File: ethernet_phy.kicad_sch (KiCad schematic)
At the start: 25 parts, among them J2 RJ45_Abracon_ARJP11A-MASA-B-A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, U1 RTL8201F

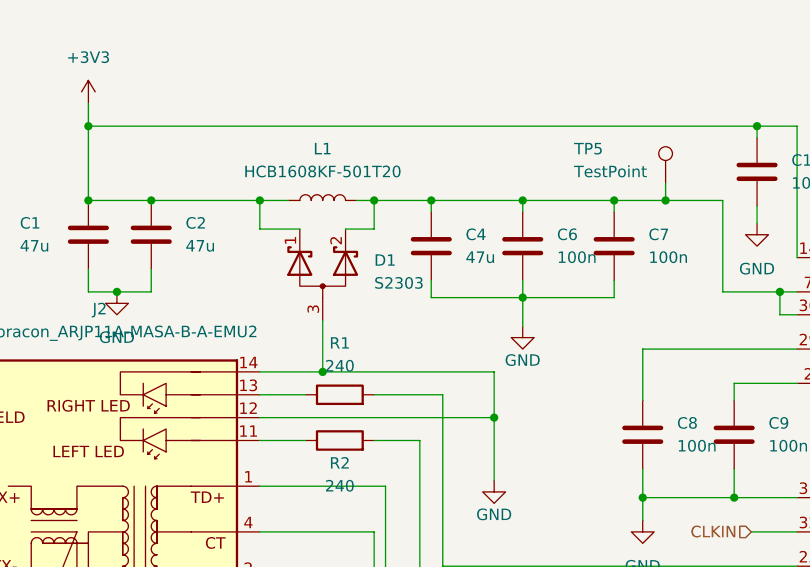
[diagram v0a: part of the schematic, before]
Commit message: Add more LCSC markings, change to electrolytic caps :
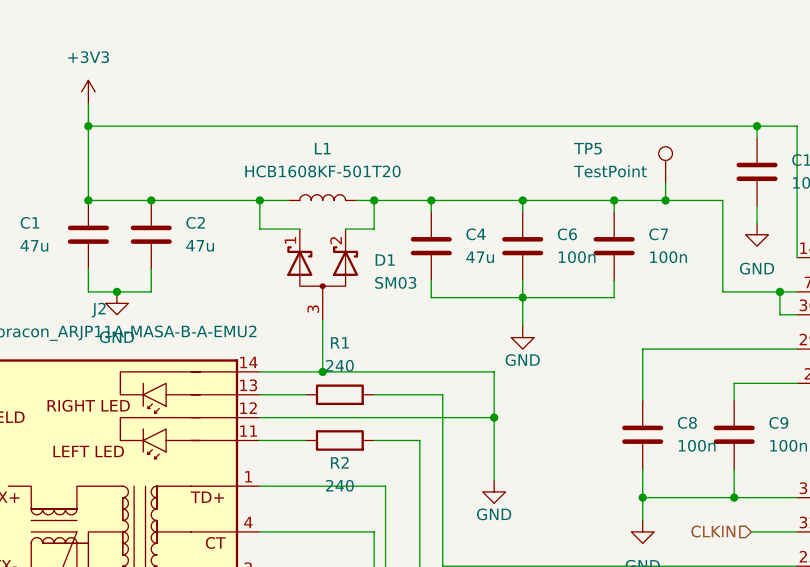
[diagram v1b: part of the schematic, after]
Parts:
- D1: value S2303 -> SM03; LCSC (none) -> C502558
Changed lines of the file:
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@@
       (effects (font (size 1.27 1.27)) (justify right))
     )
-    (property "Value" "S2303" (id 1) (at 92.075 57.4674 90)
+    (property "Value" "SM03" (id 1) (at 92.075 57.4674 90)
       (effects (font (size 1.27 1.27)) (justify right))
     )
@@
       (effects (font (size 1.27 1.27)) hide)
     )
-    (property "Datasheet" "https://www.smc-diodes.com/propdf/S2303%20THRU%20S2336%20N0291%20REV.B.pdf" (id 3) (at 86.36 57.785 0)
+    (property "Datasheet" "https://datasheet.lcsc.com/lcsc/2004071010_MDD-Microdiode-Electronics--SM03_C502558.pdf" (id 3) (at 86.36 57.785 0)
       (effects (font (size 1.27 1.27)) hide)
     )
+    (property "LCSC" "C502558" (id 4) (at 86.36 56.515 90)
+      (effects (font (size 1.27 1.27)) hide)
+    )
+    (property "Field5" "" (id 5) (at 86.36 56.515 90)
+      (effects (font (size 1.27 1.27)) hide)
+    )

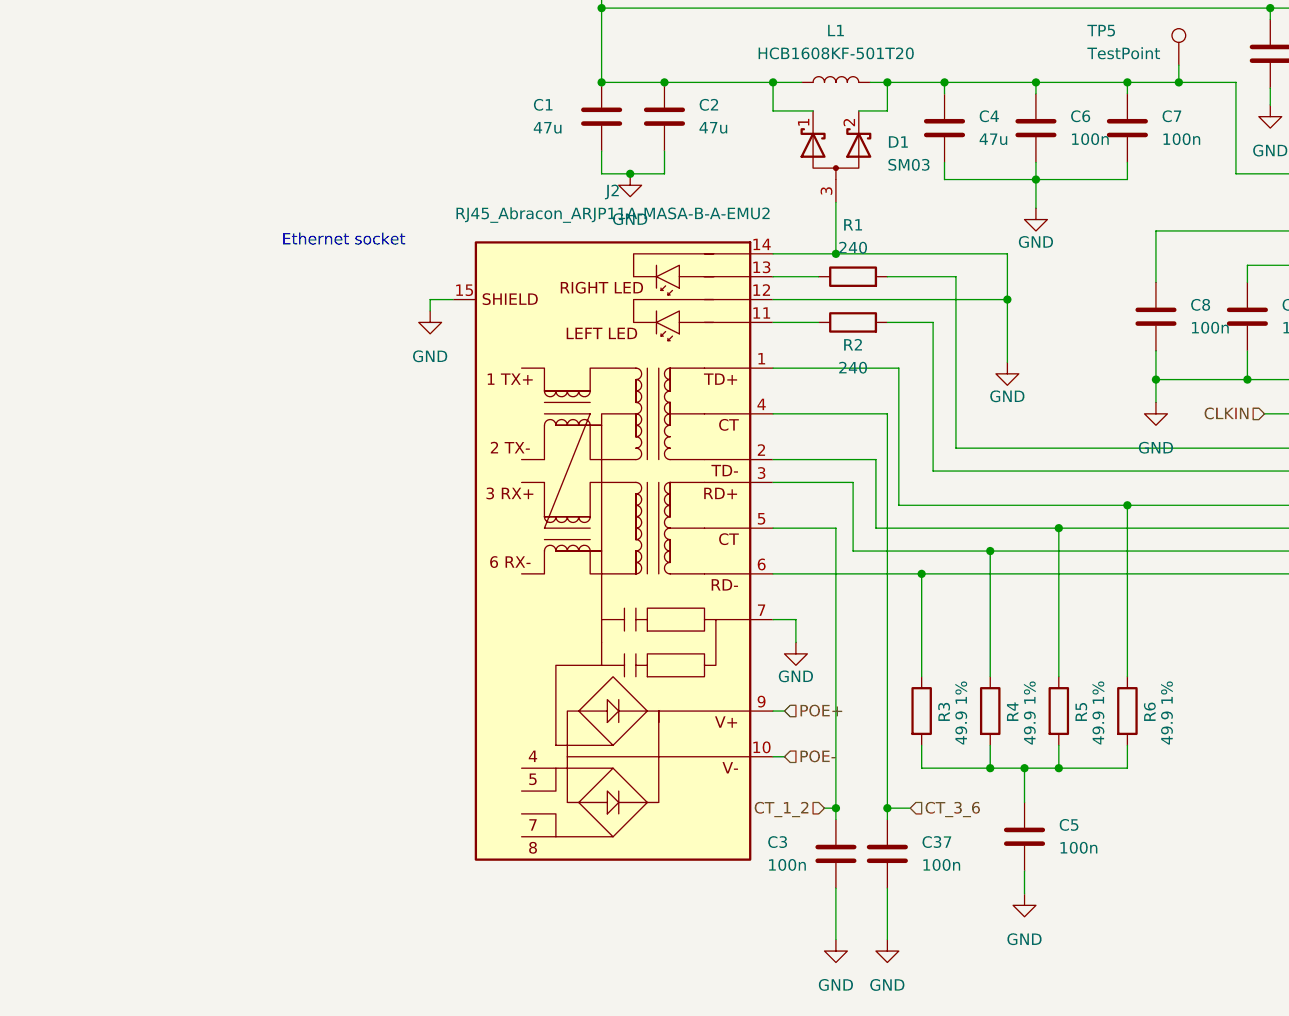
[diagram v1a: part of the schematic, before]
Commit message: Switch to LCSC RJ45 socket
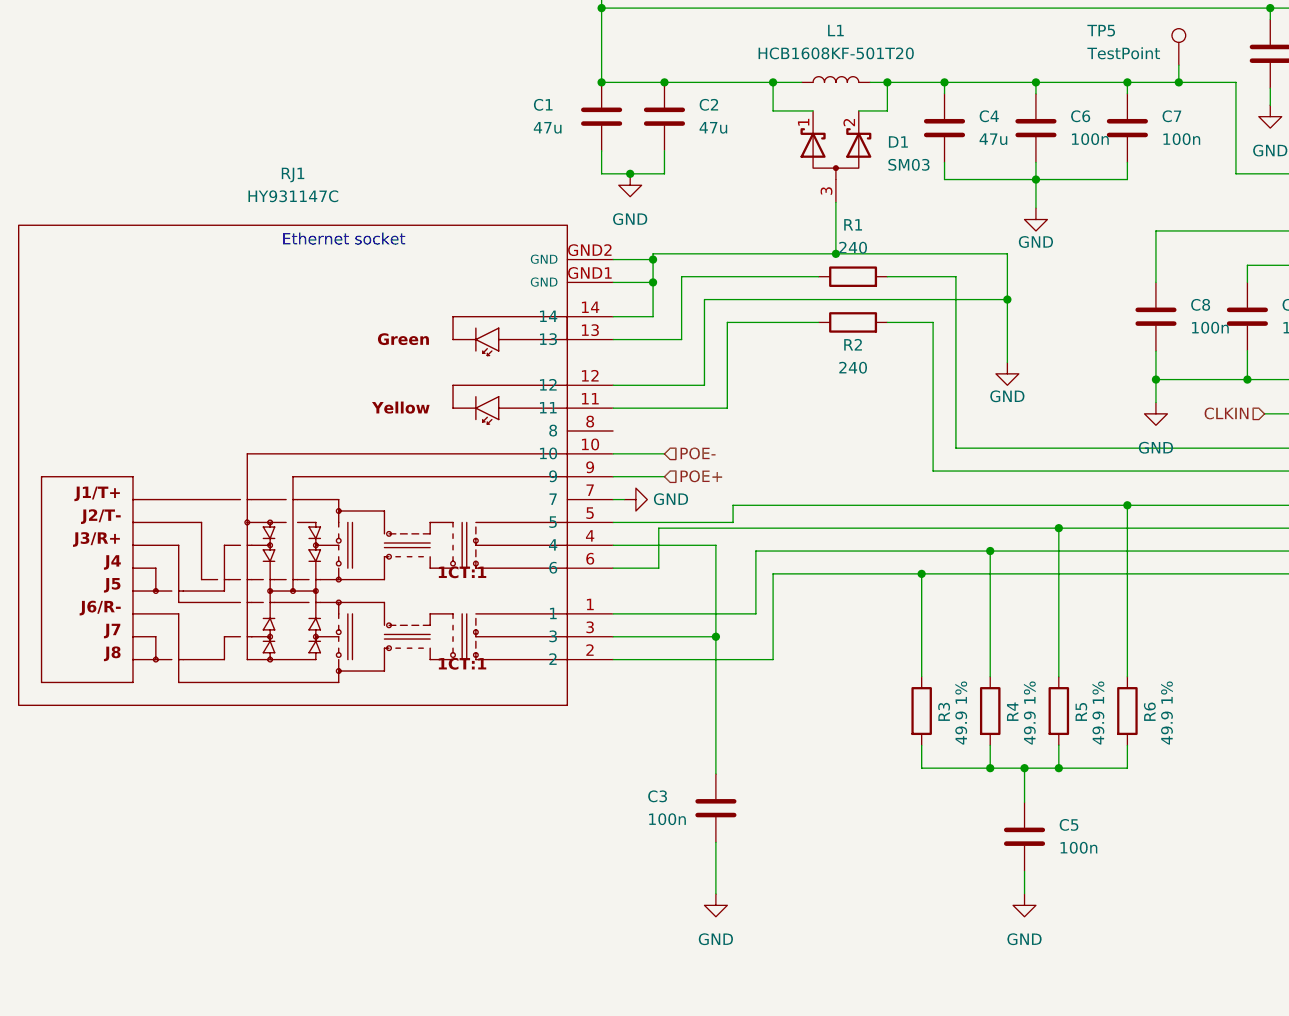
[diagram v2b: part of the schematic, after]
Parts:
- removed C37: 100n, Capacitor_SMD:C_0603_1608Metric_Pad1.08x0.95mm_HandSolder, symbol Device:C
- removed J2: RJ45_Abracon_ARJP11A-MASA-B-A-EMU2, Connector_RJ:RJ45_Abracon_ARJP11A-MA_Horizontal, symbol Connector:RJ45_Abracon_ARJP11A-MASA-B-A-EMU2
- added RJ1: HY931147C, kicad_lceda:RJ45-TH_HY931147C, symbol HY931147C:HY931147C
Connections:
- net GND: now also RJ1.12, RJ1.14, RJ1.7, RJ1.GND1 (GND), RJ1.GND2 (GND)
- net POE+: now also RJ1.9
- net POE-: now also RJ1.10
- net at R1.1: now also RJ1.13
- net at R4.1, U1.5 (MDI1+): now also RJ1.1
- net at R6.1, U1.3 (MDI0+): now also RJ1.5
- net at R5.1, U1.4 (MDI0-): now also RJ1.6
- net at R3.1, U1.6 (MDI1-): now also RJ1.2
- net at R2.1: now also RJ1.11
- net CT_1_2: no longer names the net of C3.1
- net CT_1_2: now also RJ1.3, RJ1.4
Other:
- moved on the sheet: C3

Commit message: Kicad updates, added missing resistances
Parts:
- RJ1: footprint kicad_lceda:RJ45-TH_HY931147C -> project specific:RJ45-TH_HY931147C; LCSC C356979 -> (none)
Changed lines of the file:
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@@
 			)
 		)
-		(property "Datasheet" "https://datasheet.lcsc.com/lcsc/2111021030_FOJAN-FRC0603J241-TS_C2907130.pdf"
+		(property "Datasheet" ""
 			(at 88.265 69.85 0)
 			(effects
@@
 			)
 		)
-		(property "Datasheet" "https://www.verical.com/datasheet/realtek-semiconductor-phy-rtl8201f-vb-cg-2635458.pdf"
+		(property "Datasheet" ""
 			(at 155.575 91.44 0)
 			(effects
@@
 			)
 		)
-		(property "Datasheet" "https://datasheet.lcsc.com/lcsc/1811021312_YAGEO-RC0603FR-0749R9L_C114625.pdf"
+		(property "Datasheet" ""
 			(at 95.885 118.11 0)
 			(effects
@@
 			)
 		)
-		(property "Datasheet" "https://datasheet.lcsc.com/lcsc/2111021030_FOJAN-FRC0603J241-TS_C2907130.pdf"
+		(property "Datasheet" ""
 			(at 88.265 74.93 0)
 			(effects
@@
 			)
 		)
-		(property "Footprint" "kicad_lceda:RJ45-TH_HY931147C"
+		(property "Footprint" "project specific:RJ45-TH_HY931147C"
 			(at 29.845 114.935 0)
 			(effects
@@
 			)
 		)
-		(property "Datasheet" "http://www.szlcsc.com/product/details_92943.html"
+		(property "Datasheet" ""
 			(at 29.845 109.855 0)
 			(effects
@@
 		(property "uuid" "std:f7c1c3cfb5254655a18a1e7db5808191"
 			(at 29.845 104.775 0)
-			(effects
-				(font
-					(size 1.27 1.27)
-				)
-				(hide yes)
-			)
-		)
-		(property "LCSC" "C356979"
-			(at 29.845 90.805 0)
 			(effects
 				(font
@@
 			)
 		)
-		(property "Datasheet" "https://datasheet.lcsc.com/lcsc/2009171138_TAI-TECH-HCB1608KF-501T20_C356979.pdf"
+		(property "Datasheet" ""
 			(at 86.36 48.26 0)
 			(effects
@@
 			)
 		)
-		(property "Datasheet" "https://datasheet.lcsc.com/lcsc/2004071010_MDD-Microdiode-Electronics--SM03_C502558.pdf"
+		(property "Datasheet" ""
 			(at 86.36 57.785 0)
 			(effects

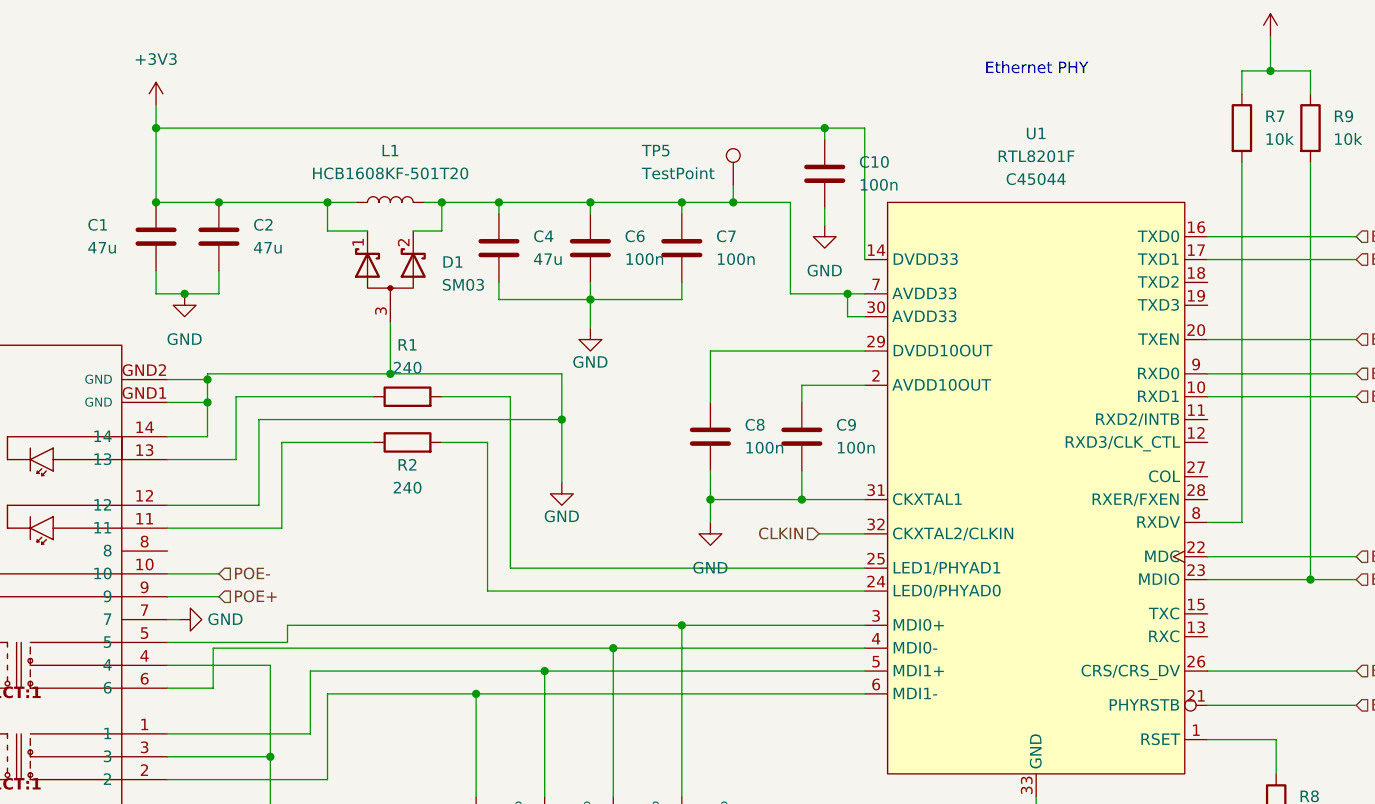
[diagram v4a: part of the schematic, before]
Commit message: Update schematic for V1.1
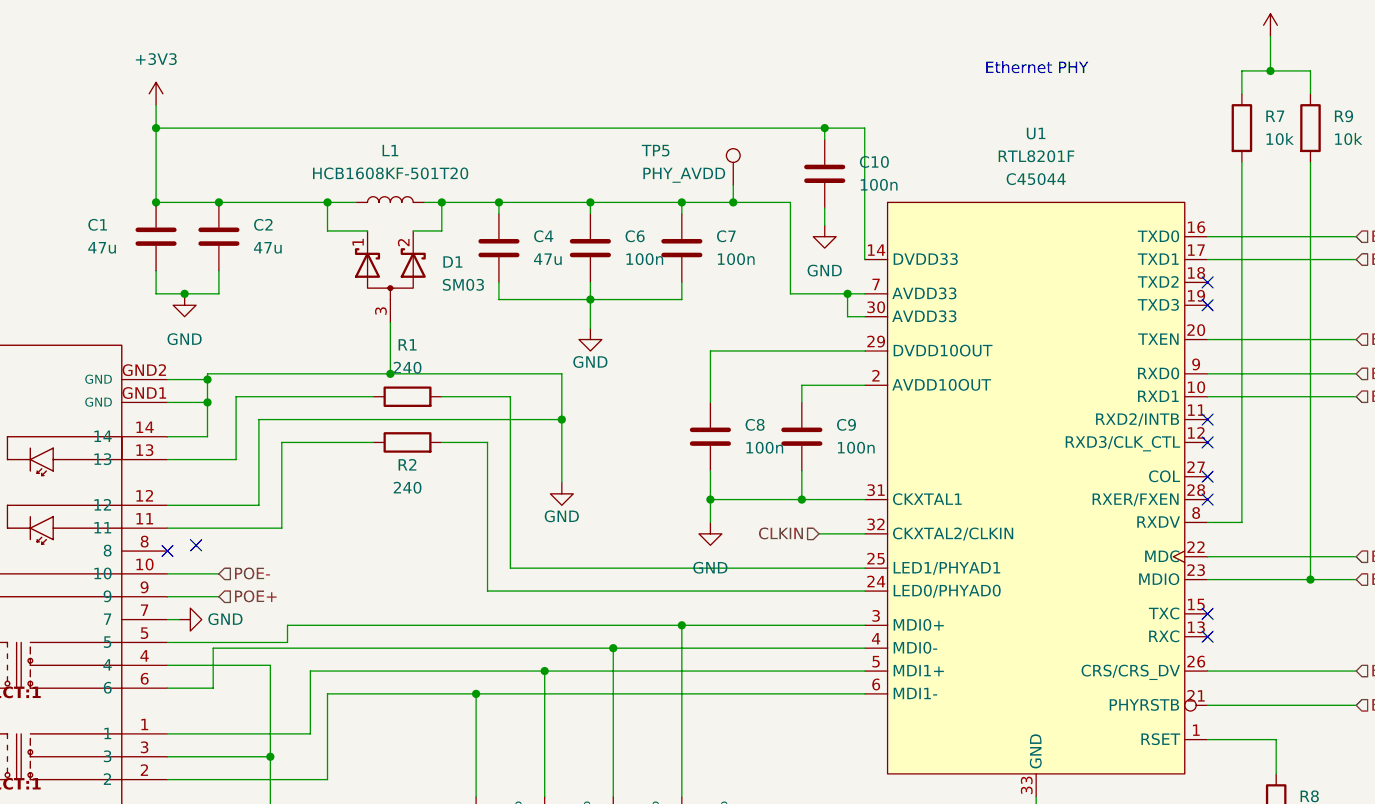
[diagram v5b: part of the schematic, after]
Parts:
- TP5: value TestPoint -> PHY_AVDD
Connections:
- no-connect marks 0 -> 10
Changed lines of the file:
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@@
 		(color 0 0 0 0)
+	)
+	(no_connect
+		(at 177.165 59.69)
+	)
+	(no_connect
+		(at 177.165 78.74)
+	)
+	(no_connect
+		(at 177.165 96.52)
+	)
+	(no_connect
+		(at 177.165 74.93)
+	)
+	(no_connect
+		(at 177.165 81.28)
+	)
+	(no_connect
+		(at 61.595 86.995)
+	)
+	(no_connect
+		(at 177.165 72.39)
+	)
+	(no_connect
+		(at 177.165 93.98)
+	)
+	(no_connect
+		(at 64.77 86.36)
+	)
+	(no_connect
+		(at 177.165 57.15)
 	)
 	(wire
@@
 			)
 		)
-		(property "Datasheet" ""
+		(property "Datasheet" "https://file.elecfans.com/web1/M00/99/0F/o4YBAF0VytaAI7ezABH66fmIRIg854.pdf?filename=RTL8201F-VB-CG.pdf"
 			(at 155.575 91.44 0)
 			(effects
@@
 			)
 		)
-		(property "Value" "TestPoint"
+		(property "Value" "PHY_AVDD"
 			(at 114.3 45.085 0)
 			(effects

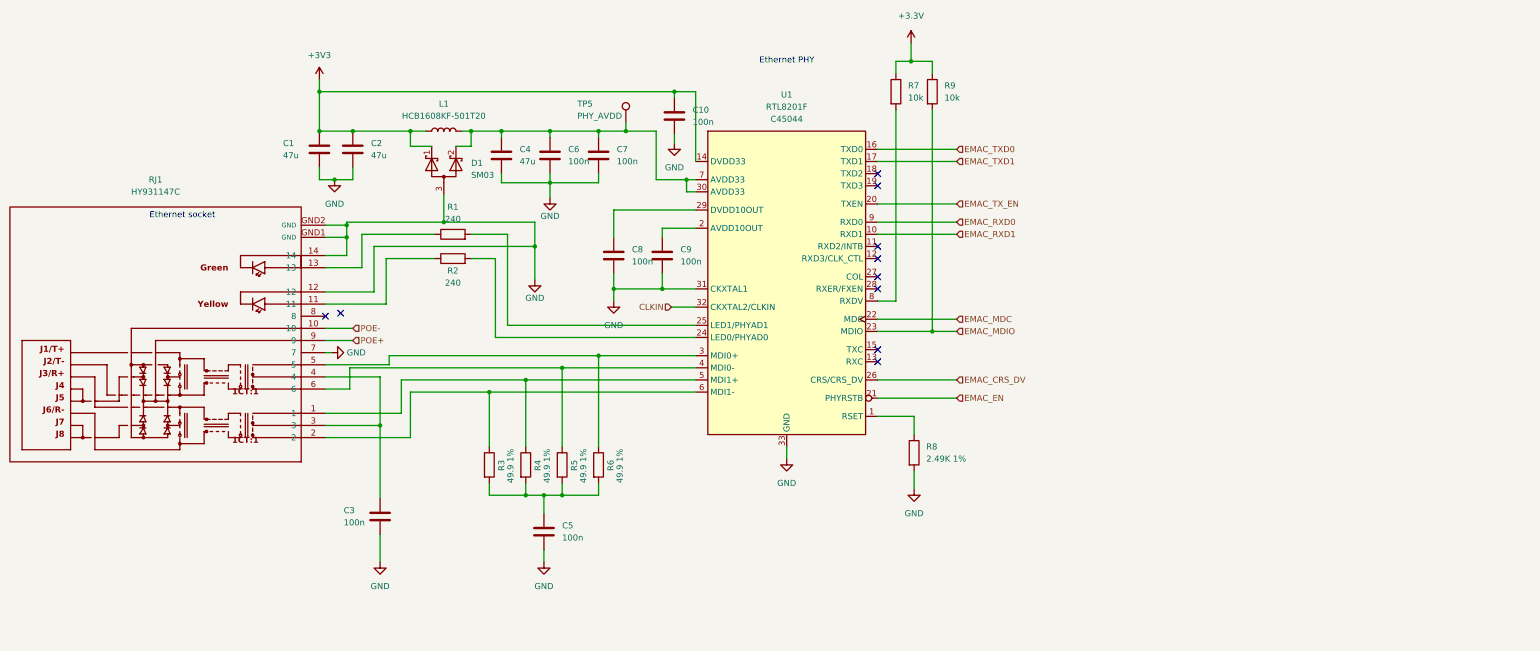
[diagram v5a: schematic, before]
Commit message: use contributed symbol for RTL8021F
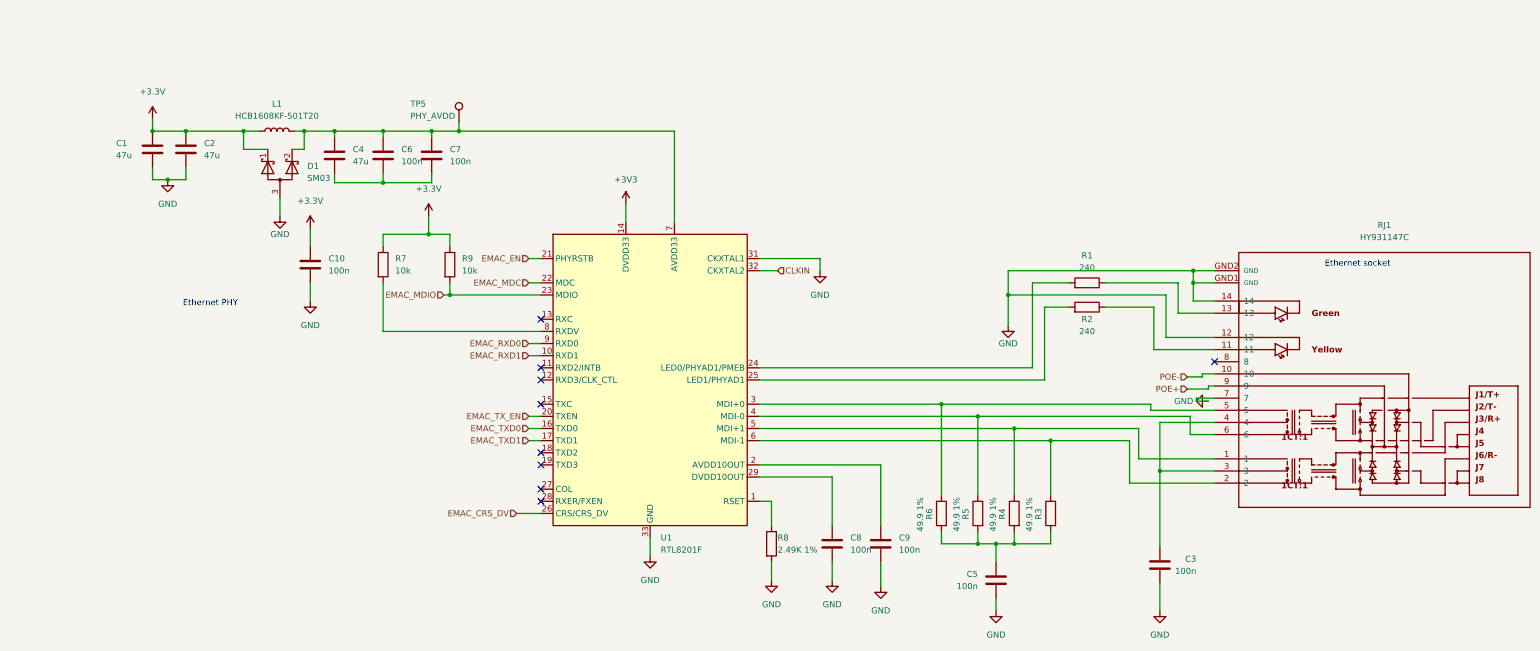
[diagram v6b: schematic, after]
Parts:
- removed U1: RTL8201F, Package_DFN_QFN:QFN-32-1EP_5x5mm_P0.5mm_EP3.3x3.3mm, symbol RTL8201F:RTL8201F
- added U1: RTL8201F, Package_DFN_QFN:QFN-32-1EP_5x5mm_P0.5mm_EP3.3x3.3mm, symbol Interface_Ethernet_Contrib:RTL8201F
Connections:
- net +3.3V: now also C1.1, C10.1, C2.1, D1.1 (K), L1.1
- net +3V3: now also U1.14 (DVDD33); no longer C1.1, C10.1, C2.1, D1.1 (K), L1.1
- net CLKIN: now also U1.32 (CKXTAL2)
- net EMAC_CRS_DV: now also U1.26 (CRS/CRS_DV)
- net EMAC_EN: now also U1.21 (PHYRSTB)
- net EMAC_MDC: now also U1.22 (MDC)
- net EMAC_MDIO: now also U1.23 (MDIO)
- net EMAC_RXD0: now also U1.9 (RXD0)
- net EMAC_RXD1: now also U1.10 (RXD1)
- net EMAC_TXD0: now also U1.16 (TXD0)
- net EMAC_TXD1: now also U1.17 (TXD1)
- net EMAC_TX_EN: now also U1.20 (TXEN)
- net GND: now also U1.31 (CKXTAL1), U1.33 (GND); no longer C4.2, C6.2, C7.2
- net at C4.1, C6.1, C7.1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: now also U1.30 (AVDD33), U1.7 (AVDD33)
- net at R1.2: now also U1.24 (LED0/PHYAD1/PMEB)
- net at R7.2: now also U1.8 (RXDV)
- net at R4.1, RJ1.1: now also U1.5 (MDI+1)
- net at R8.1: now also U1.1 (RSET)
- net at C9.1: now also U1.2 (AVDD10OUT)
- net at R2.2: now also U1.25 (LED1/PHYAD1)
- net at C8.1: now also U1.29 (DVDD10OUT)
- net at R6.1, RJ1.5: now also U1.3 (MDI+0)
- net at R5.1, RJ1.6: now also U1.4 (MDI-0)
- net at R3.1, RJ1.2: now also U1.6 (MDI-1)
- new net: C4.2, C6.2, C7.2
- no-connect marks 10 -> 9
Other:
- moved on the sheet: C1, C10, C2, C3, C4, C5, C6, C7, C8, C9, D1, L1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
